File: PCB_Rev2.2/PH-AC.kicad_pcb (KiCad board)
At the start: 2 copper layers, 200 x 100 mm, 61 parts, among them J1 USB_C_Receptacle_USB2.0_14P, J2 Conn_01x03, Q1 DMG1012T, SW1 SW_Push, SW10 SW_Push, SW2 RotaryEncoder_Switch_MP, SW3 RotaryEncoder_Switch_MP, SW4 SW_Push, SW5 SW_Push, SW6 SW_Push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

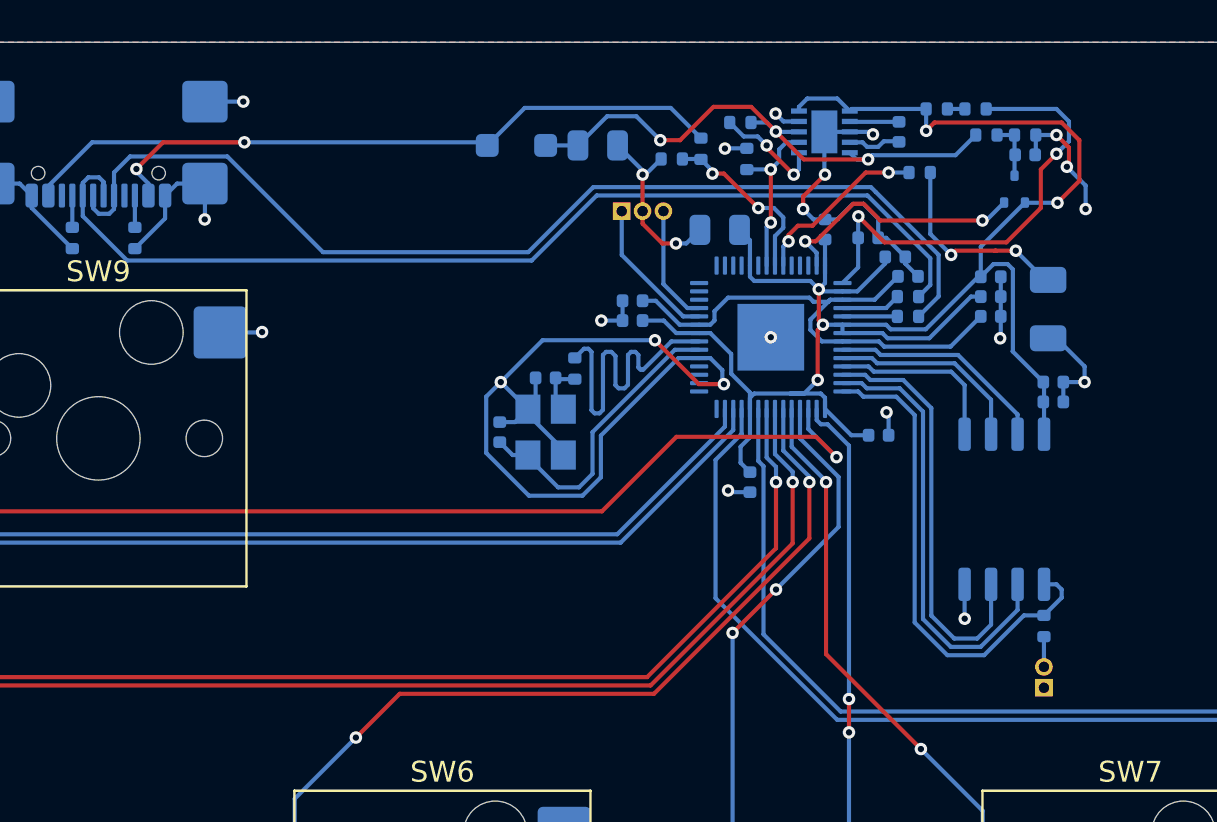
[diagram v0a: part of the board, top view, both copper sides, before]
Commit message: LDO Modification
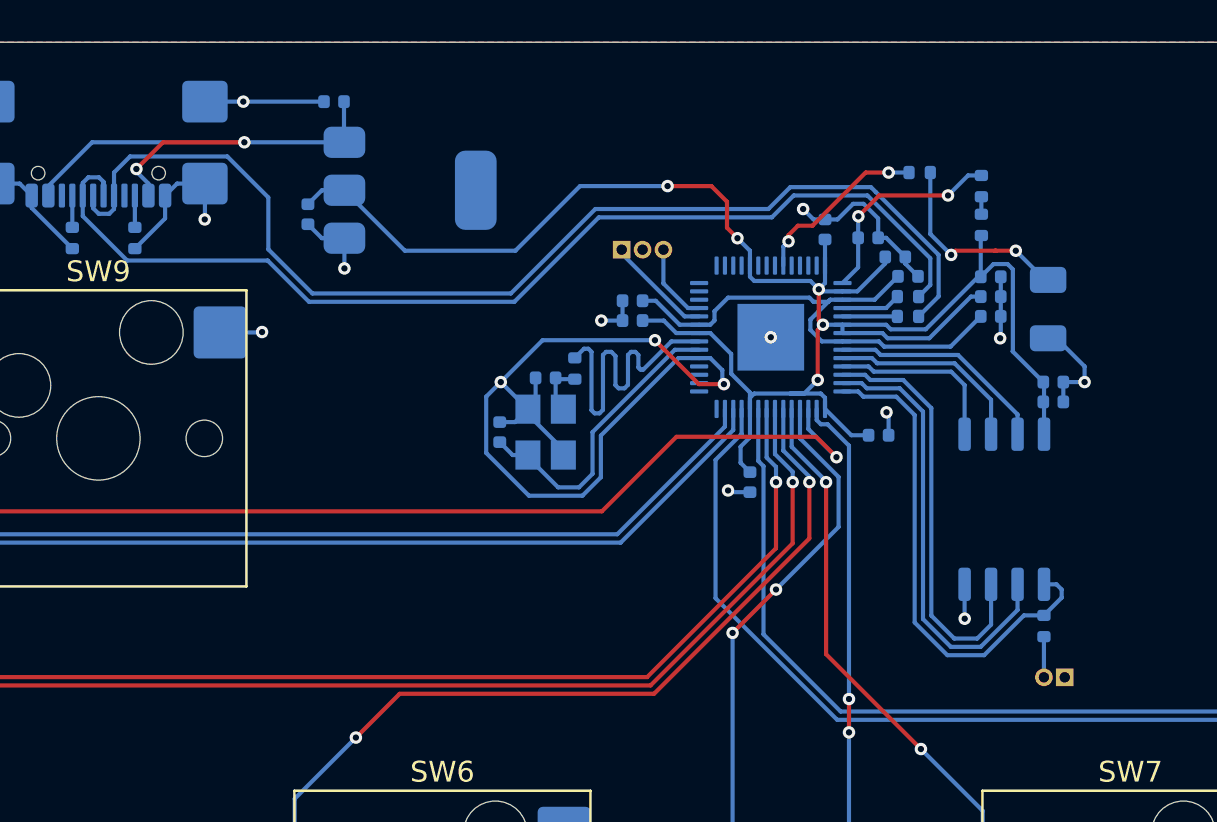
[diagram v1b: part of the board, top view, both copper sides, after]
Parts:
- removed C16: 1n, Capacitor_SMD:C_0402_1005Metric
- removed D1: MBR120VLSFT1G, Diode_SMD:D_SOD-123F
- removed L1: 2u2, Capacitor_SMD:C_0402_1005Metric
- removed Q1: DMG1012T, Package_TO_SOT_SMD:SOT-523
- removed R10, R11: R, Resistor_SMD:R_0402_1005Metric
- removed R5: 5K6, Resistor_SMD:R_0402_1005Metric
- removed R6: 10K, Resistor_SMD:R_0402_1005Metric
- removed R7, R8: 100K, Resistor_SMD:R_0402_1005Metric
- C12, C13: value 47u -> 10u; footprint Capacitor_SMD:C_0805_2012Metric -> Capacitor_SMD:C_0402_1005Metric
- U2: value RT6150B-33GQW -> NCP1117-3.3_SOT223; footprint footprints:10-WFDFN-EP_RIT -> Package_TO_SOT_SMD:SOT-223
- moved U2 20.1 mm to (182.4, 60.1), turned to 0 degrees
- moved C13 19.8 mm to (177.6, 61.2), turned to -90 degrees
- moved C12 12.8 mm to (178.8, 55.9), turned to 180 degrees
- moved R2 5.96 mm to (209.8, 61.8), turned to 90 degrees
- moved R1 3.71 mm to (209.8, 59.9), turned to 90 degrees
- moved J2 1.85 mm to (192.6, 63.0)
- moved SW1 1.12 mm to (213.8, 83.5), turned to 90 degrees
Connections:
- C12 pad 1: /VSYS -> VBUS
- U1 pad 35: /GPIO23 -> unconnected-(U1-GPIO23-Pad35)
- U1 pad 36: /GPIO24 -> unconnected-(U1-GPIO24-Pad36)
- U1 pad 41: /GPIO29_ADC3 -> unconnected-(U1-GPIO29_ADC3-Pad41)
- U2 pad 1: +3V3 -> GND
- U2 pad 2: Net-(U2-LX2) -> +3V3
- U2 pad 3: GND -> VBUS
- U2 pad 4: Net-(U2-LX1) -> (no net)
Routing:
- net /VSYS: track 27.4 -> 0.00 mm, vias 3 -> 0
- net GND: track 120.1 -> 103.5 mm, vias 31 -> 23
- net VBUS: track 41.3 -> 24.7 mm
- net /GPIO29_ADC3: track 12.4 -> 0.00 mm, vias 2 -> 0
- net Net-(U1-ADC_AVDD): track 22.4 -> 10.2 mm
- net /GPIO24: track 8.55 -> 0.00 mm, vias 2 -> 0
- net /GPIO23: track 8.07 -> 0.00 mm, vias 2 -> 0
- net Net-(U2-EN): track 5.32 -> 0.00 mm, vias 2 -> 0
- net /USB_DP: track 51.3 -> 54.4 mm
- net Net-(Q1-D): track 2.79 -> 0.00 mm
- net Net-(U2-LX1): track 2.58 -> 0.00 mm
- net Net-(U2-LX2): track 2.37 -> 0.00 mm
- net Net-(J2-Pin_1): track 7.04 -> 5.15 mm
- net Net-(J2-Pin_3): track 5.69 -> 3.82 mm
- net +3V3: track 89.7 -> 91.4 mm
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
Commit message: Detail Update
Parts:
- J2: footprint Connector_PinHeader_1.00mm:PinHeader_1x03_P1.00mm_Vertical -> Connector_PinHeader_2.54mm:PinHeader_1x03_P2.54mm_Vertical
- SW1: footprint Connector_PinHeader_1.00mm:PinHeader_1x02_P1.00mm_Vertical -> Button_Switch_THT:SW_PUSH_6mm
- moved J2 13.6 mm to (183.0, 72.7), turned to 90 degrees
- moved C1 11.1 mm to (199.3, 62.1)
- moved SW1 7.78 mm to (221.4, 81.6)
- moved R9 0.40 mm to (212.4, 81.0)
- moved R1 0.31 mm to (209.9, 59.6)
- moved R2 0.31 mm to (209.9, 61.5)
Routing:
- net Net-(J2-Pin_3): track 3.82 -> 22.3 mm
- net Net-(J2-Pin_1): track 5.15 -> 17.4 mm
- net Net-(R9-Pad1): track 1.95 -> 11.0 mm
- net +3V3: track 91.4 -> 86.9 mm
- net GND: track 103.5 -> 106.7 mm, vias 23 -> 24
- net Net-(D2-A): track 9.78 -> 8.72 mm
- net /USB_DP: track 54.4 -> 55.2 mm
- net /USB_DM: track 51.8 -> 52.7 mm
- net /QSPI_SS: track 24.1 -> 23.3 mm
- net /QSPI_SD2: track 20.4 -> 21.0 mm
- net /QSPI_SD1: track 21.4 -> 22.1 mm

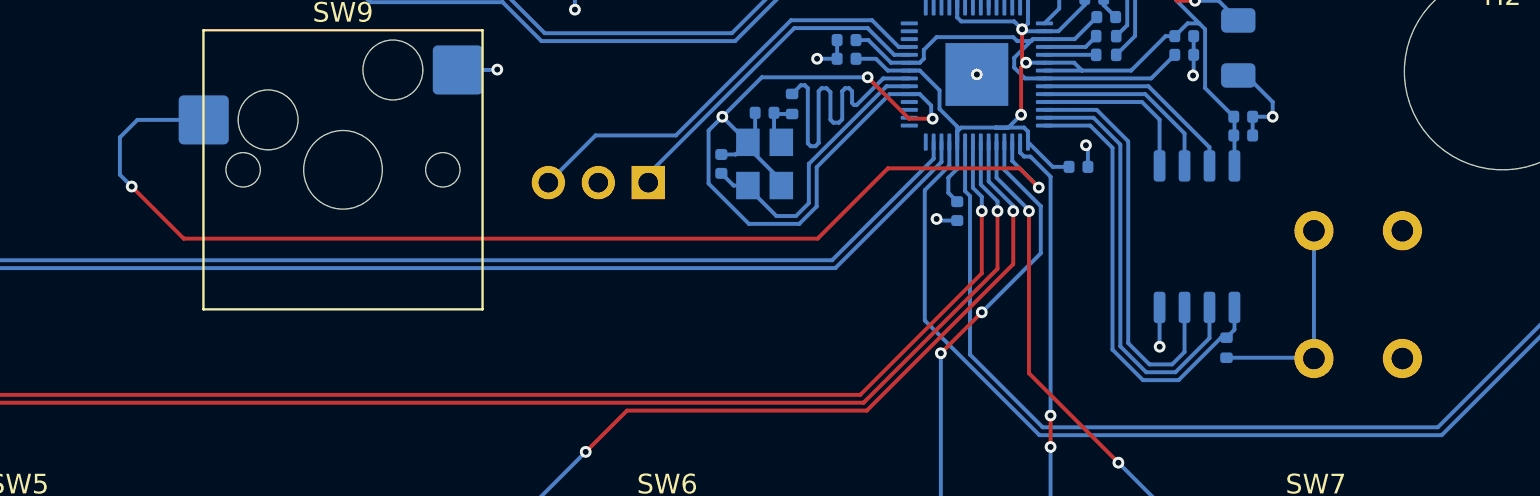
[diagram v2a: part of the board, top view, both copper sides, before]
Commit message: Changing Footprint
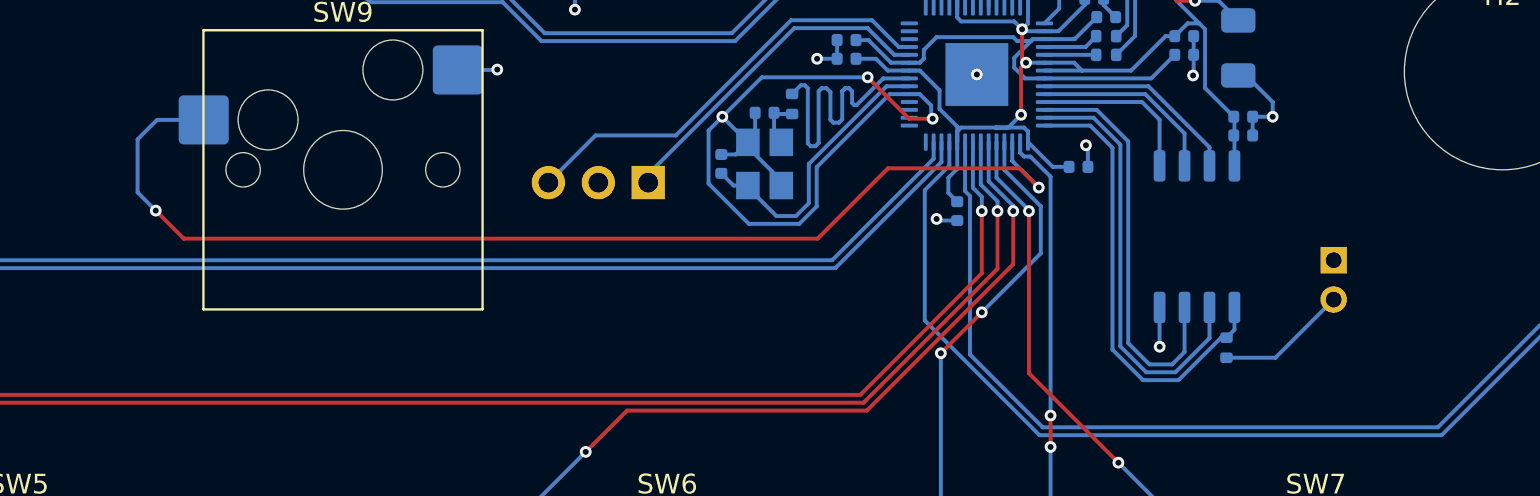
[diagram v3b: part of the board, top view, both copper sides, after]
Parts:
- SW1: footprint Button_Switch_THT:SW_PUSH_6mm -> Connector_PinHeader_2.00mm:PinHeader_1x02_P2.00mm_Vertical
- moved SW1 6.10 mm to (217.9, 76.6), turned to 180 degrees
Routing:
- net Net-(R9-Pad1): track 11.0 -> 6.68 mm
- net BT5: track 59.5 -> 58.2 mm
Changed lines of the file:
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@@
 		)
 	)
-	(footprint "Button_Switch_THT:SW_PUSH_6mm"
+	(footprint "Connector_PinHeader_2.00mm:PinHeader_1x02_P2.00mm_Vertical"
 		(layer "B.Cu")
-		(at 221.4 81.6 90)
-		(descr "Generic 6mm SW tactile push button")
-		(tags "tact sw push 6mm")
+		(at 217.9 76.6 180)
+		(descr "Through hole straight pin header, 1x02, 2.00mm pitch, single row")
+		(tags "Through hole pin header THT 1x02 2.00mm single row")
 		(property "Reference" "SW1"
-			(at 3.25 2 -90)
+			(at 0 2.06 0)
 			(layer "B.SilkS")
 			(effects
@@
 		)
 		(property "Value" "SW_Push"
-			(at 3.75 -6.7 -90)
+			(at 0 -4.06 0)
 			(layer "B.Fab")
 			(effects
@@
 			)
 		)
-		(property "Footprint" "Button_Switch_THT:SW_PUSH_6mm"
-			(at 0 0 -90)
+		(property "Footprint" "Connector_PinHeader_2.00mm:PinHeader_1x02_P2.00mm_Vertical"
+			(at 0 0 0)
 			(unlocked yes)
 			(layer "B.Fab")
@@
 		)
 		(property "Datasheet" ""
-			(at 0 0 -90)
+			(at 0 0 0)
 			(unlocked yes)
 			(layer "B.Fab")
@@
 		)
 		(property "Description" "Push button switch, generic, two pins"
-			(at 0 0 -90)
+			(at 0 0 0)
 			(unlocked yes)
 			(layer "B.Fab")
@@
 		)
 		(property "Sim.Device" ""
-			(at 0 0 90)
+			(at 0 0 180)
 			(unlocked yes)
 			(layer "B.Fab")
@@
 		)
 		(property "Sim.Pins" ""
-			(at 0 0 90)
+			(at 0 0 180)
 			(unlocked yes)
 			(layer "B.Fab")
@@
 		(attr through_hole)
 		(fp_line
-			(start 5.5 -5.5)
-			(end 1 -5.5)
+			(start 1.06 -1)
+			(end -1.06 -1)
 			(stroke
 				(width 0.12)
@@
 		)
 		(fp_line
-			(start -0.25 -3)
-			(end -0.25 -1.5)
+			(start 1.06 -3.06)
+			(end 1.06 -1)
 			(stroke
 				(width 0.12)
@@
 		)
 		(fp_line
-			(start 6.75 -1.5)
-			(end 6.75 -3)
+			(start 1.06 -3.06)
+			(end -1.06 -3.06)
 			(stroke
 				(width 0.12)
@@
 		)
 		(fp_line
-			(start 1 1)
-			(end 5.5 1)
+			(start 0 1.06)
+			(end -1.06 1.06)
 			(stroke
 				(width 0.12)
@@
 		)
 		(fp_line
-			(start 8 -6)
-			(end 7.75 -6)
-			(stroke
-				(width 0.05)
-				(type solid)
-			)
-			(layer "B.CrtYd")
-		)
-		(fp_line
-			(start -1.25 -6)
-			(end 7.75 -6)
-			(stroke
-				(width 0.05)
-				(type solid)
-			)
-			(layer "B.CrtYd")
-		)
-		(fp_line
-			(start -1.25 -6)
-			(end -1.5 -6)
-			(stroke
-				(width 0.05)
-				(type solid)
-			)
-			(layer "B.CrtYd")
-		)
-		(fp_line
-			(start -1.5 -6)
-			(end -1.5 -5.75)
+			(start -1.06 1.06)
+			(end -1.06 0)
 			(stroke
-				(width 0.05)
-				(type solid)
-			)
-			(layer "B.CrtYd")
-		)
-		(fp_line
-			(start 8 -5.75)
-			(end 8 -6)
-			(stroke
-				(width 0.05)
-				(type solid)
-			)
-			(layer "B.CrtYd")
-		)
-		(fp_line
-			(start 8 -5.75)
-			(end 8 1.25)
-			(stroke
-				(width 0.05)
+				(width 0.12)
 				(type solid)
 			)
-			(layer "B.CrtYd")
+			(layer "B.SilkS")
 		)
 		(fp_line
-			(start 8 1.25)
-			(end 8 1.5)
+			(start -1.06 -3.06)
+			(end -1.06 -1)
 			(stroke
-				(width 0.05)
+				(width 0.12)
 				(type solid)
 			)
-			(layer "B.CrtYd")
+			(layer "B.SilkS")
 		)
 		(fp_line
-			(start -1.5 1.25)
-			(end -1.5 -5.75)
+			(start 1.5 1.5)
+			(end 1.5 -3.5)
 			(stroke
 				(width 0.05)
@@
 		)
 		(fp_line
-			(start 8 1.5)
-			(end 7.75 1.5)
+			(start 1.5 -3.5)
+			(end -1.5 -3.5)
 			(stroke
 				(width 0.05)
@@
 		)
 		(fp_line
-			(start 7.75 1.5)
-			(end -1.25 1.5)
+			(start -1.5 1.5)
+			(end 1.5 1.5)
 			(stroke
 				(width 0.05)
@@
 		)
 		(fp_line
-			(start -1.25 1.5)
+			(start -1.5 -3.5)
 			(end -1.5 1.5)
 			(stroke
@@
 		)
 		(fp_line
-			(start -1.5 1.5)
-			(end -1.5 1.25)
-			(stroke
-				(width 0.05)
-				(type solid)
-			)
-			(layer "B.CrtYd")
-		)
-		(fp_line
-			(start 6.25 -5.25)
-			(end 6.25 0.75)
+			(start 1 1)
+			(end -0.5 1)
 			(stroke
 				(width 0.1)
@@
 		)
 		(fp_line
-			(start 0.25 -5.25)
-			(end 6.25 -5.25)
+			(start 1 -3)
+			(end 1 1)
 			(stroke
 				(width 0.1)
@@
 		)
 		(fp_line
-			(start 6.25 0.75)
-			(end 3.25 0.75)
+			(start -0.5 1)
+			(end -1 0.5)
 			(stroke
 				(width 0.1)
@@
 		)
 		(fp_line
-			(start 3.25 0.75)
-			(end 0.25 0.75)
+			(start -1 0.5)
+			(end -1 -3)
 			(stroke
 				(width 0.1)
@@
 		)
 		(fp_line
-			(start 0.25 0.75)
-			(end 0.25 -5.25)
+			(start -1 -3)
+			(end 1 -3)
 			(stroke
 				(width 0.1)
@@
 			(layer "B.Fab")
 		)
-		(fp_circle
-			(center 3.25 -2.25)
-			(end 1.25 -2.5)
-			(stroke
-				(width 0.1)
-				(type solid)
-			)
-			(fill none)
-			(layer "B.Fab")
-		)
 		(fp_text user "${REFERENCE}"
-			(at 3.25 -2.25 -90)
+			(at 0 -1 90)
 			(layer "B.Fab")
 			(effects
@@
 			)
 		)
-		(pad "1" thru_hole circle
-			(at 0 0)
-			(size 2 2)
-			(drill 1.1)
-			(layers "*.Cu" "*.Mask")
-			(remove_unused_layers no)
-			(net 57 "GND")
-			(pinfunction "1")
-			(pintype "passive")
-		)
-		(pad "1" thru_hole circle
-			(at 6.5 0)
-			(size 2 2)
-			(drill 1.1)
+		(pad "1" thru_hole rect
+			(at 0 0 180)
+			(size 1.35 1.35)
+			(drill 0.8)
 			(layers "*.Cu" "*.Mask")
 			(remove_unused_layers no)
@@
 			(pintype "passive")
 		)
-		(pad "2" thru_hole circle
-			(at 0 -4.5)
-			(size 2 2)
-			(drill 1.1)
-			(layers "*.Cu" "*.Mask")
-			(remove_unused_layers no)
-			(net 19 "Net-(R9-Pad1)")
-			(pinfunction "2")
-			(pintype "passive")
-		)
-		(pad "2" thru_hole circle
-			(at 6.5 -4.5)
-			(size 2 2)
-			(drill 1.1)
+		(pad "2" thru_hole oval
+			(at 0 -2 180)
+			(size 1.35 1.35)
+			(drill 0.8)
 			(layers "*.Cu" "*.Mask")
 			(remove_unused_layers no)
@@
 			(pintype "passive")
 		)
-		(model "${KICAD8_3DMODEL_DIR}/Button_Switch_THT.3dshapes/SW_PUSH_6mm.wrl"
+		(model "${KICAD8_3DMODEL_DIR}/Connector_PinHeader_2.00mm.3dshapes/PinHeader_1x02_P2.00mm_Vertical.wrl"
 			(offset
 				(xyz 0 0 0)
@@
 		)
 		(fp_text user "${REFERENCE}"
-			(at 0 -2.54 360)
+			(at 0 -2.54 0)
 			(layer "B.Fab")
 			(effects
@@
 	)
 	(segment
-		(start 212.45 81.56)
-		(end 216.86 81.56)
+		(start 214.94 81.56)
+		(end 212.45 81.56)
 		(width 0.2)
 		(layer "B.Cu")
@@
 	)
 	(segment
-		(start 216.9 81.6)
-		(end 216.9 75.1)
-		(width 0.2)
-		(layer "B.Cu")
-		(net 19)
-	)
-	(segment
-		(start 216.86 81.56)
-		(end 216.9 81.6)
+		(start 217.9 78.6)
+		(end 214.94 81.56)
 		(width 0.2)
 		(layer "B.Cu")
@@
 	)
 	(segment
-		(start 191.65 75.5)
-		(end 159.4 75.5)
+		(start 201.923491 71.924963)
+		(end 202.9 72.901472)
 		(width 0.2)
 		(layer "F.Cu")
@@
 	)
 	(segment
-		(start 201.923491 71.924963)
-		(end 195.225037 71.924963)
+		(start 159.4 75.5)
+		(end 191.65 75.5)
 		(width 0.2)
 		(layer "F.Cu")
@@
 	)
 	(segment
-		(start 159.4 75.5)
-		(end 156.75 72.85)
+		(start 195.225037 71.924963)
+		(end 201.923491 71.924963)
 		(width 0.2)
 		(layer "F.Cu")
@@
 	)
 	(segment
-		(start 195.225037 71.924963)
-		(end 191.65 75.5)
+		(start 157.975 74.075)
+		(end 159.4 75.5)
 		(width 0.2)
 		(layer "F.Cu")
@@
 	)
 	(segment
-		(start 202.9 72.901472)
-		(end 201.923491 71.924963)
+		(start 191.65 75.5)
+		(end 195.225037 71.924963)
 		(width 0.2)
 		(layer "F.Cu")
@@
 	)
 	(via
-		(at 156.75 72.85)
+		(at 157.975 74.075)
 		(size 0.6)
 		(drill 0.3)
@@
 	)
 	(segment
-		(start 156.75 72.85)
-		(end 156.15 72.25)
+		(start 157.05 73.15)
+		(end 157.05 70.45)
 		(width 0.2)
 		(layer "B.Cu")
@@
 	)
 	(segment
-		(start 156.15 70.35)
-		(end 157.04 69.46)
+		(start 157.05 70.45)
+		(end 158.04 69.46)
 		(width 0.2)
 		(layer "B.Cu")
@@
 	)
 	(segment
-		(start 157.04 69.46)
+		(start 158.04 69.46)
 		(end 160.415 69.46)
 		(width 0.2)
@@
 	)
 	(segment
-		(start 202.9 72.901472)
-		(end 201.55 71.551472)
+		(start 157.975 74.075)
+		(end 157.05 73.15)
 		(width 0.2)
 		(layer "B.Cu")
@@
 	)
 	(segment
-		(start 160.5 69.545)
-		(end 160.415 69.46)
+		(start 202.9 72.901472)
+		(end 201.55 71.551472)
 		(width 0.2)
 		(layer "B.Cu")
@@
 	)
 	(segment
-		(start 156.15 72.25)
-		(end 156.15 70.35)
+		(start 160.5 69.545)
+		(end 160.415 69.46)
 		(width 0.2)
 		(layer "B.Cu")

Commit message: Tinkering
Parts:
- moved C12 2.58 mm to (177.1, 57.8)
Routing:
- net VBUS: track 24.7 -> 23.6 mm
- net GND: track 106.7 -> 105.7 mm
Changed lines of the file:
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@@
 	(footprint "Capacitor_SMD:C_0402_1005Metric"
 		(layer "B.Cu")
-		(at 178.8 55.85 180)
+		(at 177.05 57.75 180)
 		(descr "Capacitor SMD 0402 (1005 Metric), square (rectangular) end terminal, IPC_7351 nominal, (Body size source: IPC-SM-782 page 76, https://www.pcb-3d.com/wordpress/wp-content/uploads/ipc-sm-782a_amendment_1_and_2.pdf), generated with kicad-footprint-generator")
 		(tags "capacitor")
@@
 	)
 	(segment
-		(start 179.28 57.78)
-		(end 179.3 57.8)
+		(start 169.9 59.780001)
+		(end 169.32306 59.203061)
 		(width 0.2)
 		(layer "B.Cu")
@@
 	)
 	(segment
-		(start 169.9 59.780001)
-		(end 169.32306 59.203061)
+		(start 175.5 58.8)
+		(end 174.5 57.8)
 		(width 0.2)
 		(layer "B.Cu")
@@
 	)
 	(segment
-		(start 179.3 56.02)
-		(end 179.28 56)
+		(start 179.25 57.75)
+		(end 179.3 57.8)
 		(width 0.2)
 		(layer "B.Cu")
@@
 	)
 	(segment
-		(start 179.28 55.85)
-		(end 179.28 57.78)
+		(start 177.53 57.75)
+		(end 179.25 57.75)
 		(width 0.2)
 		(layer "B.Cu")
@@
 	)
 	(segment
-		(start 174.5 57.8)
-		(end 179.3 57.8)
+		(start 177.53 57.75)
+		(end 176.48 58.8)
+		(width 0.2)
+		(layer "B.Cu")
+		(net 7)
+	)
+	(segment
+		(start 176.48 58.8)
+		(end 175.5 58.8)
 		(width 0.2)
 		(layer "B.Cu")
@@
 	)
 	(segment
+		(start 176.35 57.75)
+		(end 176.57 57.75)
+		(width 0.2)
+		(layer "B.Cu")
+		(net 57)
+	)
+	(segment
 		(start 169.25 62.9)
 		(end 170.7 61.45)
@@
 	)
 	(segment
-		(start 174.45 55.85)
-		(end 178.32 55.85)
-		(width 0.2)
-		(layer "B.Cu")
-		(net 57)
-	)
-	(segment
 		(start 213.78 69.3)
 		(end 213.78 70.25)
@@
 		(width 0.2)
 		(layer "B.Cu")
+		(net 57)
+	)
+	(segment
+		(start 174.45 55.85)
+		(end 176.35 57.75)
+		(width 0.2)
+		(layer "B.Cu")
